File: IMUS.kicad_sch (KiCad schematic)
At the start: 12 parts, among them U1 ICM-426788P, U10 BNO055, Y2 OV_7604

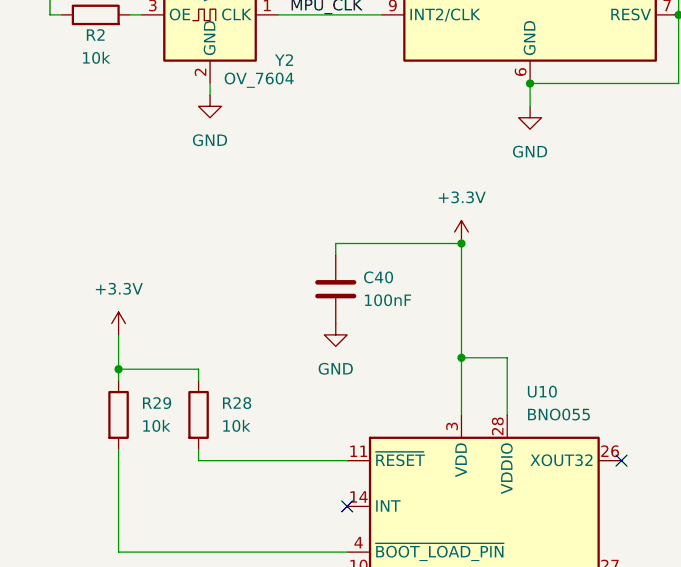
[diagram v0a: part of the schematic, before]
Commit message: Fix
- Add decoupling cap
- Component layout
- Redraw zones
- New buck converter
- Layout tweaks
- Change connector
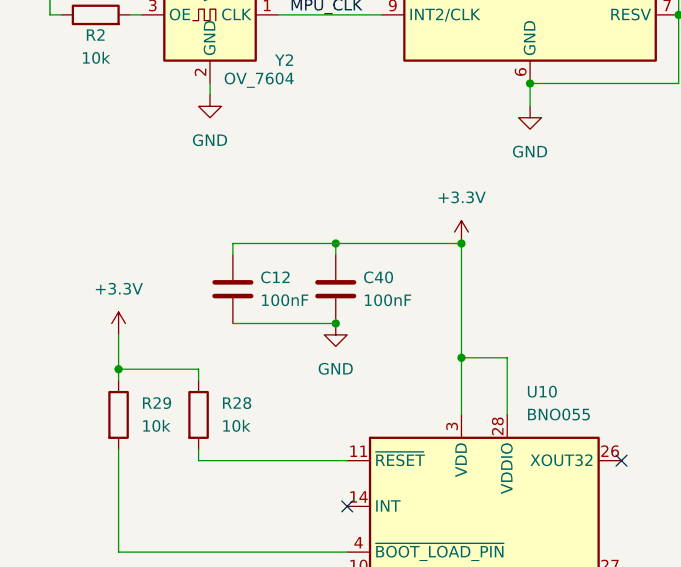
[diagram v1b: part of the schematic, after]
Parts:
- added C12: 100nF, Capacitor_SMD:C_0603_1608Metric, symbol Device:C
- C17, C18, C19, C20: footprint Capacitor_SMD:C_0603_1608Metric -> Capacitor_SMD:C_0402_1005Metric
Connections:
- net +3.3V: now also C12.1
- net GND: now also C12.2
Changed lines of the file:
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@@
+	)
+	(junction
+		(at 54.61 93.98)
+		(diameter 0)
+		(color 0 0 0 0)
 	)
 	(junction
@@
 	)
 	(junction
+		(at 54.61 85.09)
+		(diameter 0)
+		(color 0 0 0 0)
+	)
+	(junction
 		(at 95.25 29.21)
 		(diameter 0)
@@
 	(wire
 		(pts
+			(xy 43.18 85.09) (xy 54.61 85.09)
+		)
+		(stroke
+			(width 0)
+			(type default)
+		)
+	)
+	(wire
+		(pts
 			(xy 86.36 132.08) (xy 101.6 132.08)
 		)
@@
 	(wire
 		(pts
+			(xy 43.18 86.36) (xy 43.18 85.09)
+		)
+		(stroke
+			(width 0)
+			(type default)
+		)
+	)
+	(wire
+		(pts
 			(xy 55.88 134.62) (xy 55.88 146.05)
 		)
@@
 		(pts
 			(xy 71.12 146.05) (xy 73.66 146.05)
+		)
+		(stroke
+			(width 0)
+			(type default)
+		)
+	)
+	(wire
+		(pts
+			(xy 43.18 93.98) (xy 54.61 93.98)
 		)
 		(stroke
@@
 	)
 	(symbol
+		(lib_id "Device:C")
+		(at 43.18 90.17 0)
+		(unit 1)
+		(exclude_from_sim no)
+		(in_bom yes)
+		(on_board yes)
+		(dnp no)
+		(property "Reference" "C12"
+			(at 46.228 88.9 0)
+			(effects
+				(font
+					(size 1.27 1.27)
+				)
+				(justify left)
+			)
+		)
+		(property "Value" "100nF"
+			(at 46.228 91.44 0)
+			(effects
+				(font
+					(size 1.27 1.27)
+				)
+				(justify left)
+			)
+		)
+		(property "Footprint" "Capacitor_SMD:C_0603_1608Metric"
+			(at 44.1452 93.98 0)
+			(effects
+				(font
+					(size 1.27 1.27)
+				)
+				(hide yes)
+			)
+		)
+		(property "Datasheet" "~"
+			(at 43.18 90.17 0)
+			(effects
+				(font
+					(size 1.27 1.27)
+				)
+				(hide yes)
+			)
+		)
+		(property "Description" "Unpolarized capacitor"
+			(at 43.18 90.17 0)
+			(effects
+				(font
+					(size 1.27 1.27)
+				)
+				(hide yes)
+			)
+		)
+		(pin "2"
+		)
+		(pin "1"
+		)
+		(instances
+			(project "KiRA Flight Computer"
+				(path "/aff8106b-a9b7-4e48-85ad-25b2eb3ce379/8eff3ce5-9e46-4062-a747-8aaf29e42d94"
+					(reference "C12")
+					(unit 1)
+				)
+			)
+		)
+	)
+	(symbol
 		(lib_id "power:+3.3V")
 		(at 40.64 38.1 0)
@@
 			)
 		)
-		(property "Footprint" "Capacitor_SMD:C_0603_1608Metric"
+		(property "Footprint" "Capacitor_SMD:C_0402_1005Metric"
 			(at 67.0052 36.83 0)
 			(effects
@@
 			)
 		)
-		(property "Footprint" "Capacitor_SMD:C_0603_1608Metric"
+		(property "Footprint" "Capacitor_SMD:C_0402_1005Metric"
 			(at 30.1752 48.26 0)
 			(effects
@@
 			)
 		)
-		(property "Footprint" "Capacitor_SMD:C_0603_1608Metric"
+		(property "Footprint" "Capacitor_SMD:C_0402_1005Metric"
 			(at 96.2152 36.83 0)
 			(effects
@@
 			)
 		)
-		(property "Footprint" "Capacitor_SMD:C_0603_1608Metric"
+		(property "Footprint" "Capacitor_SMD:C_0402_1005Metric"
 			(at 55.5752 36.83 0)
 			(effects
